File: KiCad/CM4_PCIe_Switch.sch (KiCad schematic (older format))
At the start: 39 parts, among them IC2 PI7C9X2G404SLBFDE, U4 AP7363-10D

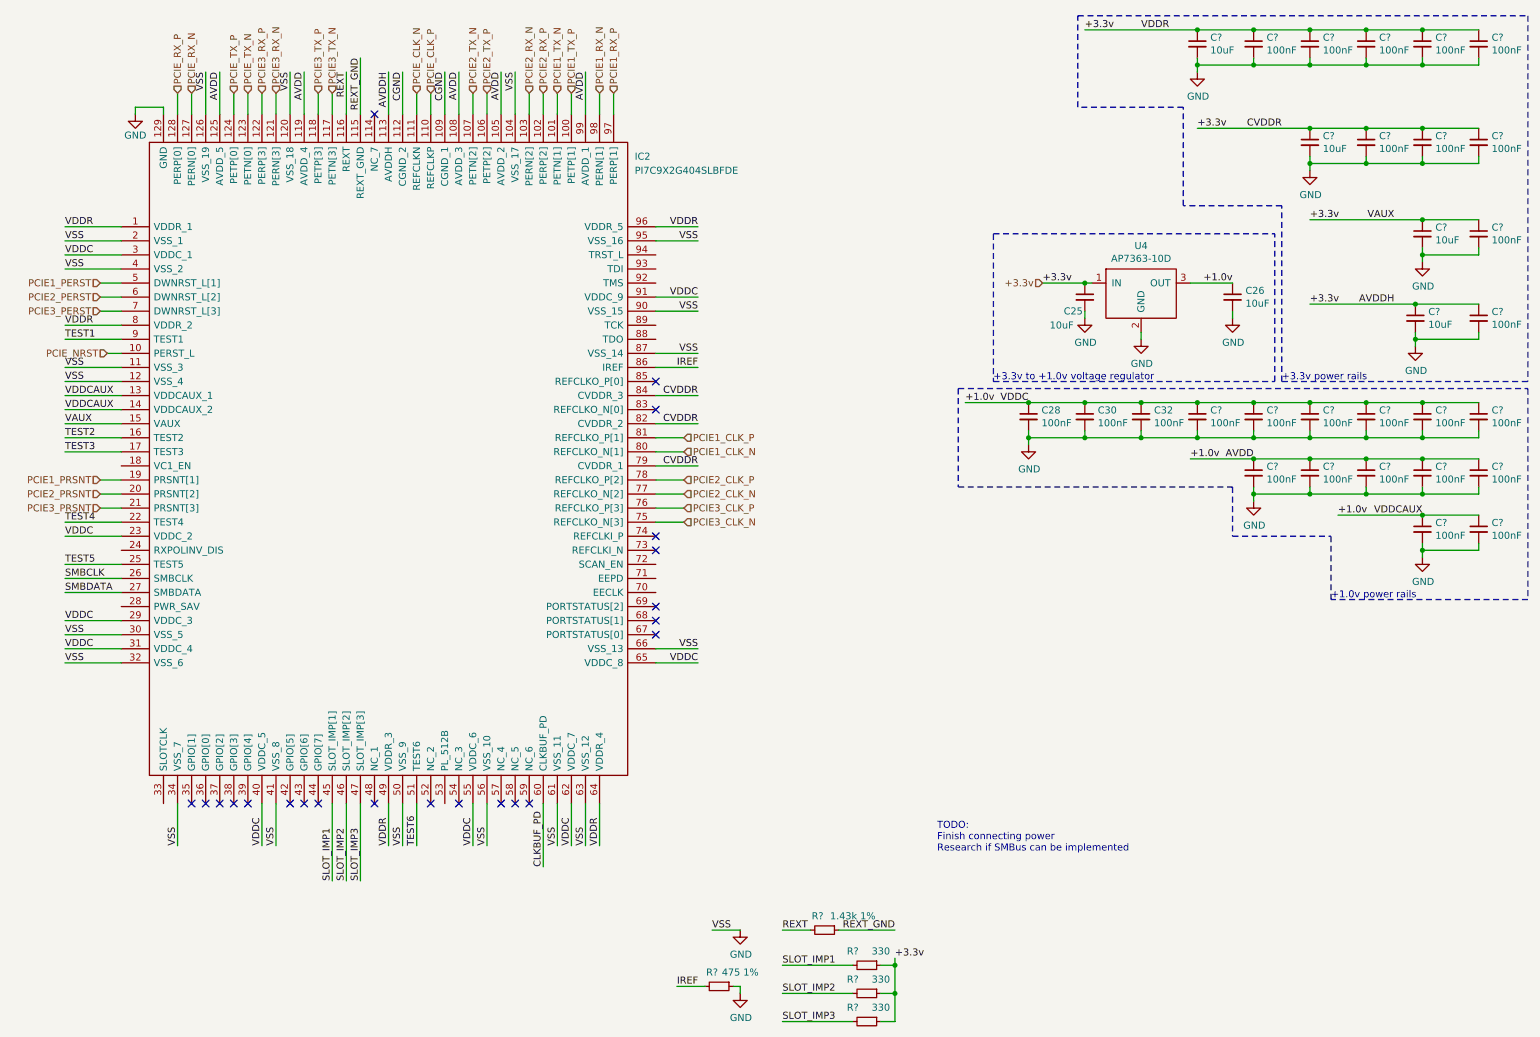
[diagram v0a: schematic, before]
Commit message: added jumper descriptions
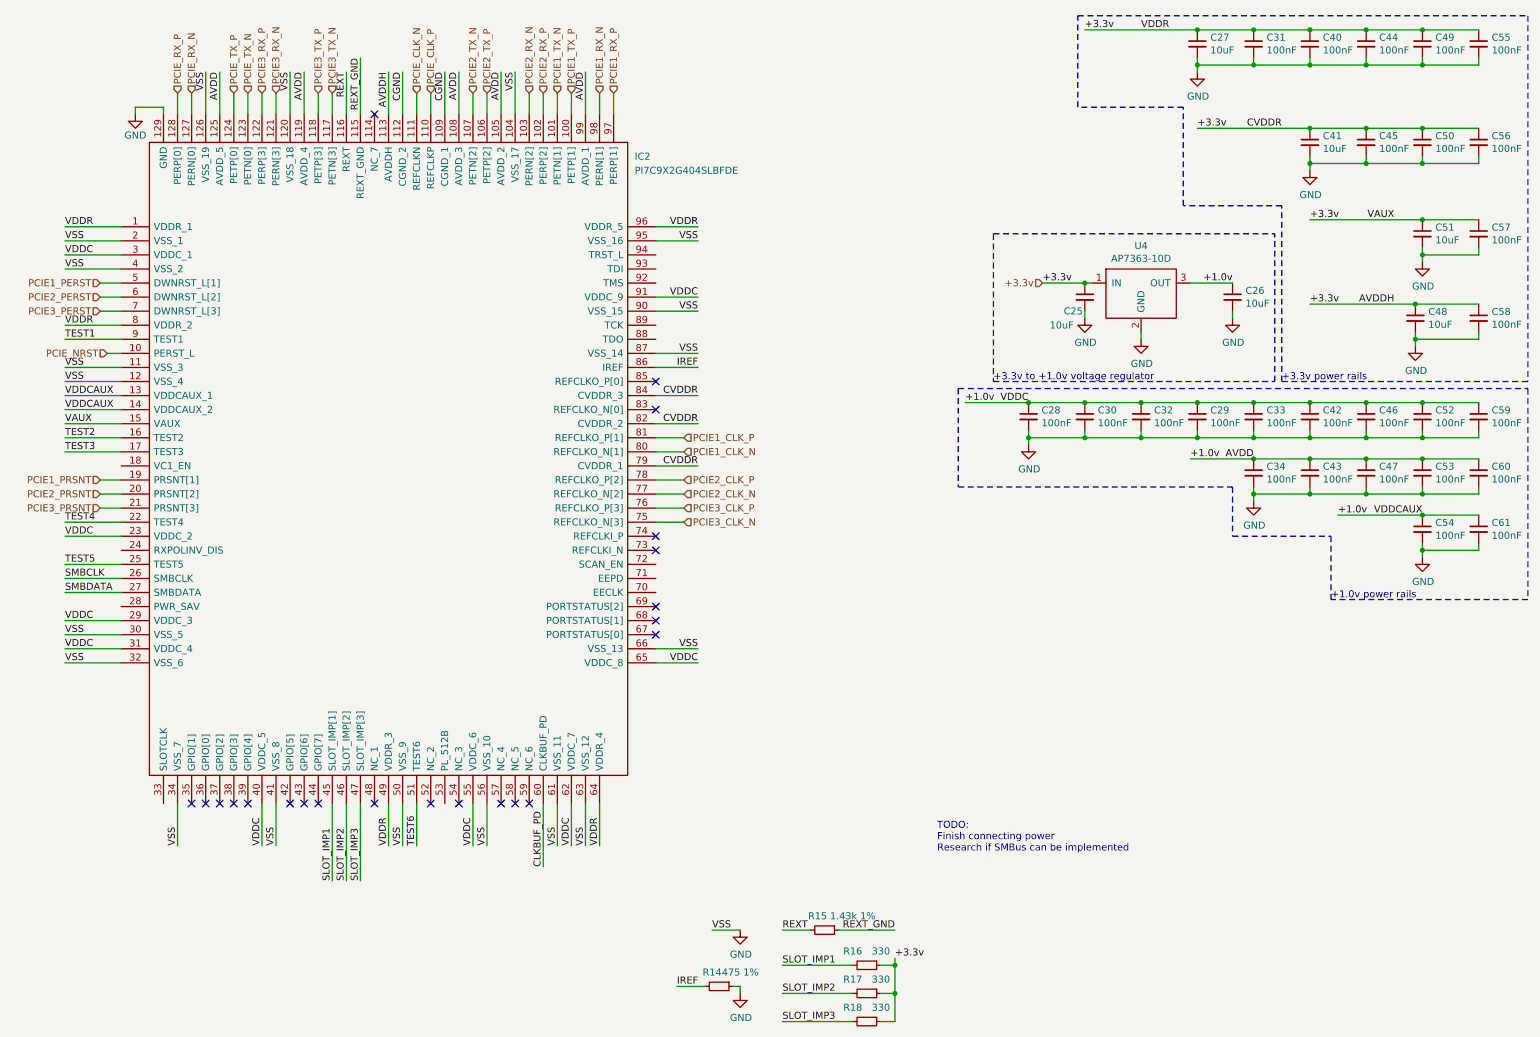
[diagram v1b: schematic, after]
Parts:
- gave numbers to parts that had none: 32

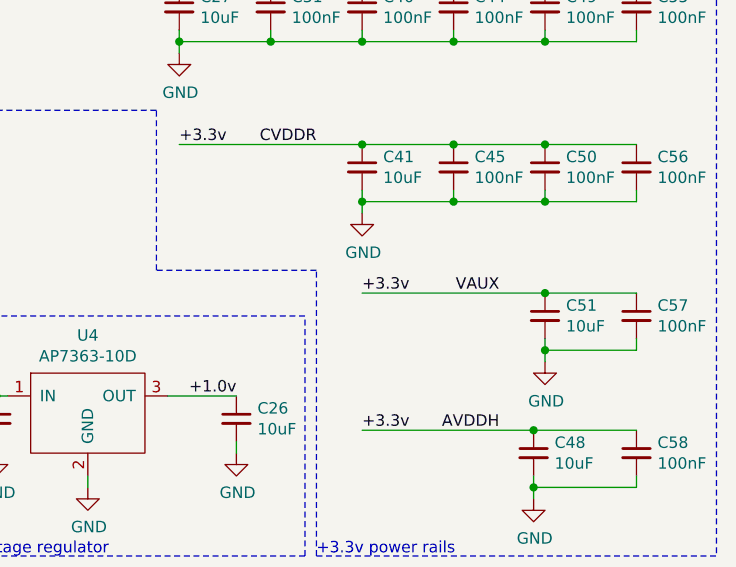
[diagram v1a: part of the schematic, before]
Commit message: Added 3.3v standby voltage regulator for PCI-e auxiliary power
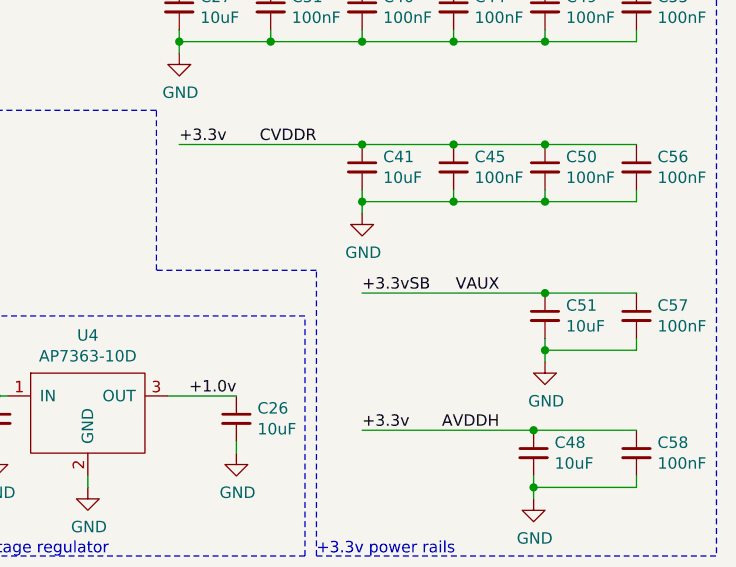
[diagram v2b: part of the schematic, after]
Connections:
- net +3.3v: no longer C51.1, C57.1, IC2.15 (VAUX)
- new net +3.3vSB: C51.1, C57.1, IC2.15 (VAUX)
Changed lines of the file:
@@
 	10850 1600 10450 1600
 Text Label 9650 2000 0    50   ~ 0
-+3.3v
++3.3vSB
 $Comp
 L Device:C_Small C51
